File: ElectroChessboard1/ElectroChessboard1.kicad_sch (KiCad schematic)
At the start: 19 parts, among them IC75 DS1307Z+T&R, J3 Conn_01x04_Pin, J5 Conn_01x06, J6 Conn_01x06, U1 ATmega2560-16A, U2 1027, Y1 Crystal, Y3 Crystal

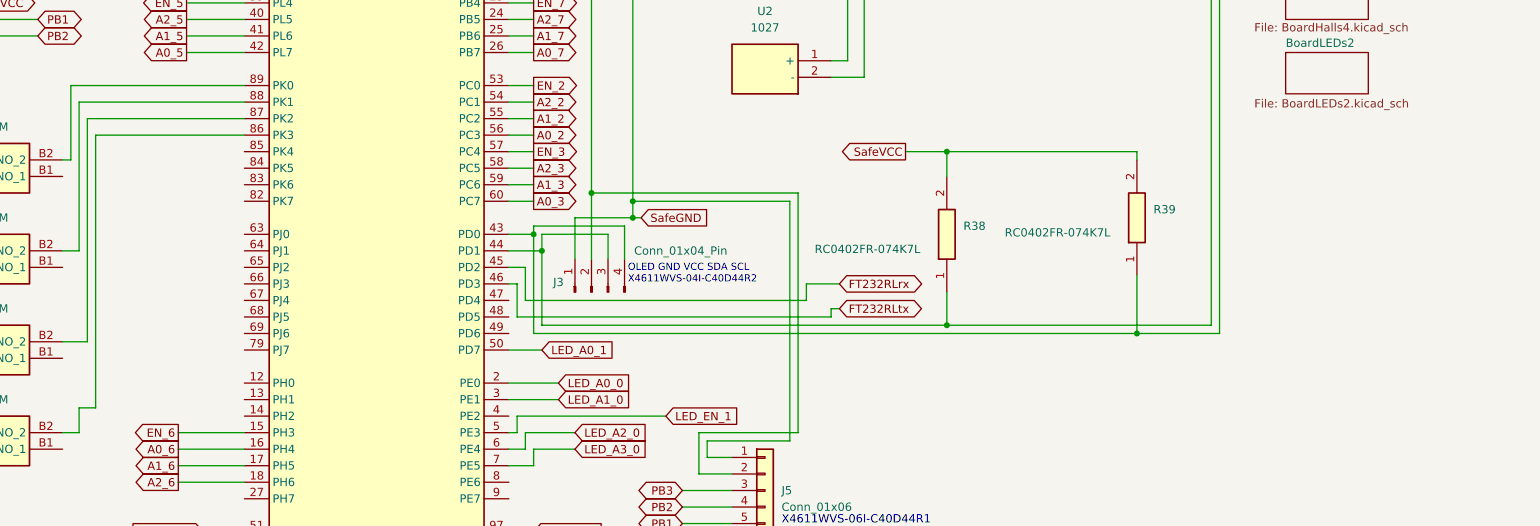
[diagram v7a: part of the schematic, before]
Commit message: Added all LEDs
Added missing 32 leds
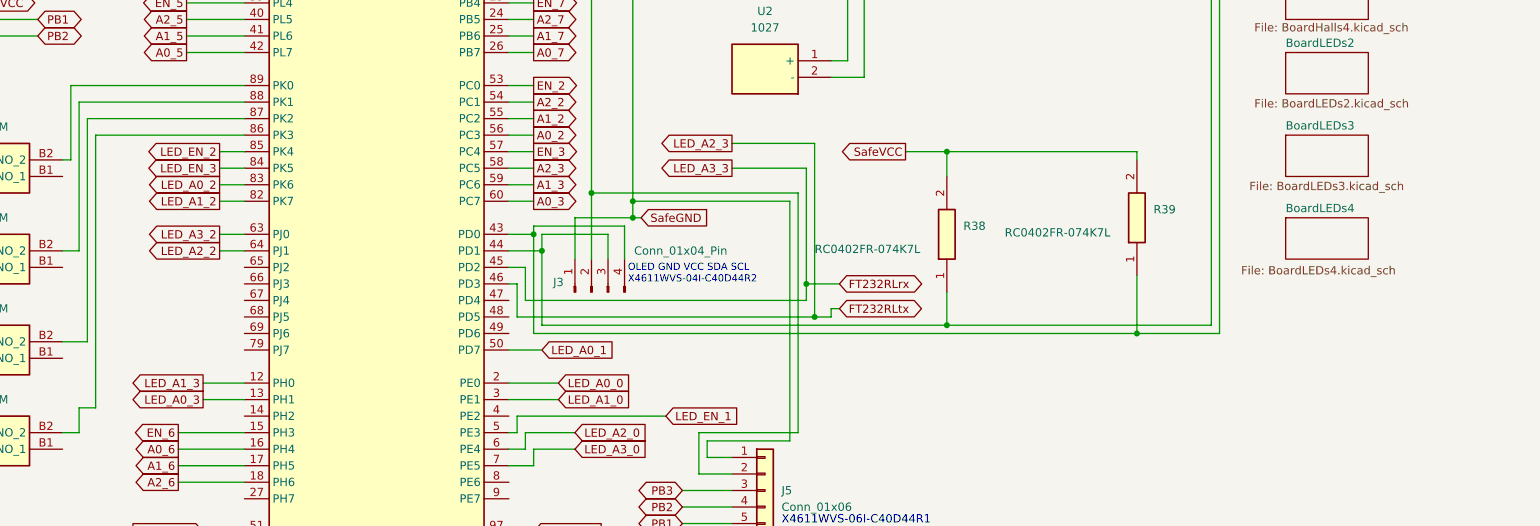
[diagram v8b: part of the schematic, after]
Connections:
- net LED_A1_3: now reaches U1.12 (PH0)
- net LED_A0_3: now reaches U1.13 (PH1)
- net LED_A3_2: now reaches U1.63 (PJ0)
- net LED_A2_2: now reaches U1.64 (PJ1)
- net LED_A1_2: now reaches U1.82 (PK7)
- net LED_A0_2: now reaches U1.83 (PK6)
- net LED_EN_3: now reaches U1.84 (PK5)
- net LED_EN_2: now reaches U1.85 (PK4)
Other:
- added sheet BoardLEDs3 (BoardLEDs3.kicad_sch)
- added sheet BoardLEDs4 (BoardLEDs4.kicad_sch)
